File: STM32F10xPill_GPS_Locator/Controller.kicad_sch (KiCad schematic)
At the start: 38 parts, among them J2 Conn_01x03, J3 Conn_01x05, SW1 SW_Push, SW3 Button A, SW4 Button B, U1 STM32F100C4T6, Y1 16MHz, Y2 32.768kHz

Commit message: Updated net names, submit schematic for feedback
After feedback is incorporated, PCB layout is ready to begin
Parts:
- C1, C10, C2, C24, C25, C3, C4, C5, C6, C7, C8, C9: footprint (none) -> Capacitor_SMD:C_0402_1005Metric
- C11: footprint (none) -> Capacitor_SMD:C_0603_1608Metric
- D1: footprint (none) -> LED_SMD:LED_0603_1608Metric
- R1, R15, R17, R2, R3, R4, R5: footprint (none) -> Resistor_SMD:R_0402_1005Metric_Pad0.72x0.64mm_HandSolder
- TP1, TP2, TP3, TP4, TP5: footprint (none) -> TestPoint:TestPoint_Pad_D1.5mm
- TP17: value GPS_1PPS -> SCK; footprint (none) -> TestPoint:TestPoint_Pad_D1.5mm
- TP18: value GPS_1PPS -> SDA; footprint (none) -> TestPoint:TestPoint_Pad_D1.5mm
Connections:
- net BUTTON_B: now reaches C24.2, R17.1, SW4.2, U1.28 (PB15)
- net BUTTON_A: now reaches C25.2, R15.1, SW3.2, U1.27 (PB14)
- no-connect marks 0 -> 16
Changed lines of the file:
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@@
 		(color 0 0 0 0)
 	)
+	(no_connect
+		(at 195.58 207.01)
+	)
+	(no_connect
+		(at 231.14 109.22)
+	)
+	(no_connect
+		(at 231.14 127)
+	)
+	(no_connect
+		(at 231.14 116.84)
+	)
+	(no_connect
+		(at 231.14 106.68)
+	)
+	(no_connect
+		(at 231.14 111.76)
+	)
+	(no_connect
+		(at 231.14 124.46)
+	)
+	(no_connect
+		(at 195.58 194.31)
+	)
+	(no_connect
+		(at 195.58 189.23)
+	)
+	(no_connect
+		(at 231.14 99.06)
+	)
+	(no_connect
+		(at 231.14 104.14)
+	)
+	(no_connect
+		(at 231.14 121.92)
+	)
+	(no_connect
+		(at 231.14 114.3)
+	)
+	(no_connect
+		(at 231.14 129.54)
+	)
+	(no_connect
+		(at 231.14 101.6)
+	)
+	(no_connect
+		(at 231.14 119.38)
+	)
 	(wire
 		(pts
@@
 		)
 	)
+	(label "SDA"
+		(at 160.02 212.09 0)
+		(effects
+			(font
+				(size 1.27 1.27)
+			)
+			(justify left bottom)
+		)
+	)
 	(label "SWDIO"
 		(at 238.76 132.08 0)
@@
 		)
 	)
+	(label "BUTTON_A"
+		(at 165.1 233.68 0)
+		(effects
+			(font
+				(size 1.27 1.27)
+			)
+			(justify left bottom)
+		)
+	)
 	(label "OSCOUT"
 		(at 138.43 140.97 0)
@@
 		)
 	)
+	(label "BUTTON_B"
+		(at 165.1 245.11 0)
+		(effects
+			(font
+				(size 1.27 1.27)
+			)
+			(justify left bottom)
+		)
+	)
 	(label "MCU_BOOT0"
 		(at 184.15 107.95 0)
@@
 		)
 	)
+	(label "SCK"
+		(at 160.02 209.55 0)
+		(effects
+			(font
+				(size 1.27 1.27)
+			)
+			(justify left bottom)
+		)
+	)
 	(global_label "SDA"
 		(shape bidirectional)
@@
 			)
 		)
-		(property "Footprint" ""
+		(property "Footprint" "Capacitor_SMD:C_0402_1005Metric"
 			(at 260.6548 76.2 0)
 			(effects
@@
 			)
 		)
-		(property "Footprint" ""
+		(property "Footprint" "Resistor_SMD:R_0402_1005Metric_Pad0.72x0.64mm_HandSolder"
 			(at 146.304 228.346 90)
 			(effects
@@
 			)
 		)
-		(property "Footprint" ""
+		(property "Footprint" "Resistor_SMD:R_0402_1005Metric_Pad0.72x0.64mm_HandSolder"
 			(at 180.594 106.934 90)
 			(effects
@@
 			)
 		)
-		(property "Footprint" ""
+		(property "Footprint" "Capacitor_SMD:C_0603_1608Metric"
 			(at 197.1548 73.66 0)
 			(effects
@@
 			)
 		)
-		(property "Footprint" ""
+		(property "Footprint" "Capacitor_SMD:C_0402_1005Metric"
 			(at 147.0152 248.92 0)
 			(effects
@@
 			)
 		)
-		(property "Footprint" ""
+		(property "Footprint" "Capacitor_SMD:C_0402_1005Metric"
 			(at 119.38 117.1448 0)
 			(effects
@@
 			)
 		)
-		(property "Footprint" ""
+		(property "Footprint" "Capacitor_SMD:C_0402_1005Metric"
 			(at 249.2248 76.2 0)
 			(effects
@@
 			)
 		)
-		(property "Footprint" ""
+		(property "Footprint" "TestPoint:TestPoint_Pad_D1.5mm"
 			(at 172.72 139.7 0)
 			(effects
@@
 			)
 		)
-		(property "Footprint" ""
+		(property "Footprint" "Capacitor_SMD:C_0402_1005Metric"
 			(at 372.4148 67.31 0)
 			(effects
@@
 			)
 		)
-		(property "Value" "GPS_1PPS"
+		(property "Value" "SCK"
 			(at 130.81 204.978 90)
 			(effects
@@
 			)
 		)
-		(property "Footprint" ""
+		(property "Footprint" "TestPoint:TestPoint_Pad_D1.5mm"
 			(at 133.35 208.28 0)
 			(effects
@@
 			)
 		)
-		(property "Footprint" ""
+		(property "Footprint" "Capacitor_SMD:C_0402_1005Metric"
 			(at 119.38 157.7848 0)
 			(effects
@@
 			)
 		)
-		(property "Footprint" ""
+		(property "Footprint" "Capacitor_SMD:C_0402_1005Metric"
 			(at 119.38 140.0048 0)
 			(effects
@@
 			)
 		)
-		(property "Footprint" ""
+		(property "Footprint" "TestPoint:TestPoint_Pad_D1.5mm"
 			(at 143.51 57.15 0)
 			(effects
@@
 			)
 		)
-		(property "Footprint" ""
+		(property "Footprint" "Resistor_SMD:R_0402_1005Metric_Pad0.72x0.64mm_HandSolder"
 			(at 114.554 202.946 90)
 			(effects
@@
 			)
 		)
-		(property "Footprint" ""
+		(property "Footprint" "Capacitor_SMD:C_0402_1005Metric"
 			(at 119.38 173.0248 0)
 			(effects
@@
 			)
 		)
-		(property "Footprint" ""
+		(property "Footprint" "TestPoint:TestPoint_Pad_D1.5mm"
 			(at 172.72 172.72 0)
 			(effects
@@
 			)
 		)
-		(property "Footprint" ""
+		(property "Footprint" "Resistor_SMD:R_0402_1005Metric_Pad0.72x0.64mm_HandSolder"
 			(at 156.464 139.954 90)
 			(effects
@@
 			)
 		)
-		(property "Footprint" ""
+		(property "Footprint" "Resistor_SMD:R_0402_1005Metric_Pad0.72x0.64mm_HandSolder"
 			(at 253.746 173.736 90)
 			(effects
@@
 			)
 		)
-		(property "Footprint" ""
+		(property "Footprint" "Resistor_SMD:R_0402_1005Metric_Pad0.72x0.64mm_HandSolder"
 			(at 156.464 228.346 90)
 			(effects
@@
 			)
 		)
-		(property "Footprint" ""
+		(property "Footprint" "Capacitor_SMD:C_0402_1005Metric"
 			(at 127 67.0052 0)
 			(effects
@@
 			)
 		)
-		(property "Footprint" ""
+		(property "Footprint" "Capacitor_SMD:C_0402_1005Metric"
 			(at 226.3648 76.2 0)
 			(effects
@@
 			)
 		)
-		(property "Footprint" ""
+		(property "Footprint" "LED_SMD:LED_0603_1608Metric"
 			(at 283.21 172.72 0)
 			(effects
@@
 			)
 		)
-		(property "Footprint" ""
+		(property "Footprint" "Resistor_SMD:R_0402_1005Metric_Pad0.72x0.64mm_HandSolder"
 			(at 106.934 202.946 90)
 			(effects
@@
 			)
 		)
-		(property "Footprint" ""
+		(property "Footprint" "Capacitor_SMD:C_0402_1005Metric"
 			(at 237.7948 76.2 0)
 			(effects
@@
 			)
 		)
-		(property "Footprint" ""
+		(property "Footprint" "TestPoint:TestPoint_Pad_D1.5mm"
 			(at 172.72 116.84 0)
 			(effects
@@
 			)
 		)
-		(property "Footprint" ""
+		(property "Footprint" "Capacitor_SMD:C_0402_1005Metric"
 			(at 159.7152 248.92 0)
 			(effects
@@
 			)
 		)
-		(property "Footprint" ""
+		(property "Footprint" "TestPoint:TestPoint_Pad_D1.5mm"
 			(at 172.72 157.48 0)
 			(effects
@@
 			)
 		)
-		(property "Value" "GPS_1PPS"
+		(property "Value" "SDA"
 			(at 137.16 204.978 90)
 			(effects
@@
 			)
 		)
-		(property "Footprint" ""
+		(property "Footprint" "TestPoint:TestPoint_Pad_D1.5mm"
 			(at 139.7 208.28 0)
 			(effects

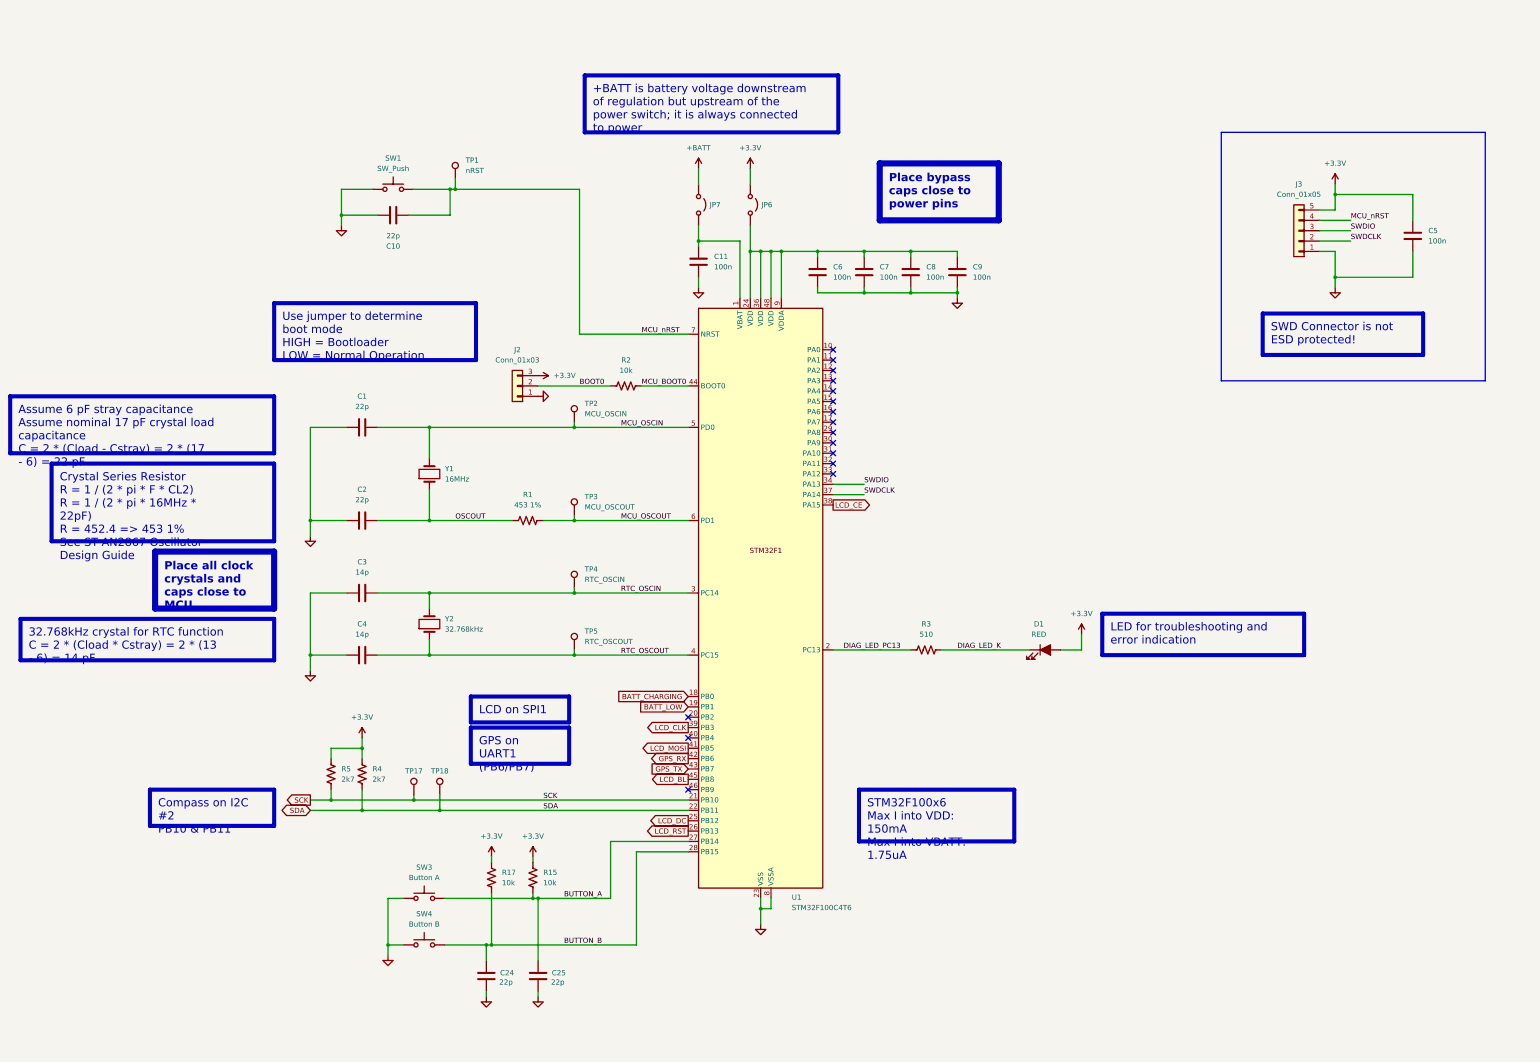
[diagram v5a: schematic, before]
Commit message: Add all footprints and symbols, retouch schametic
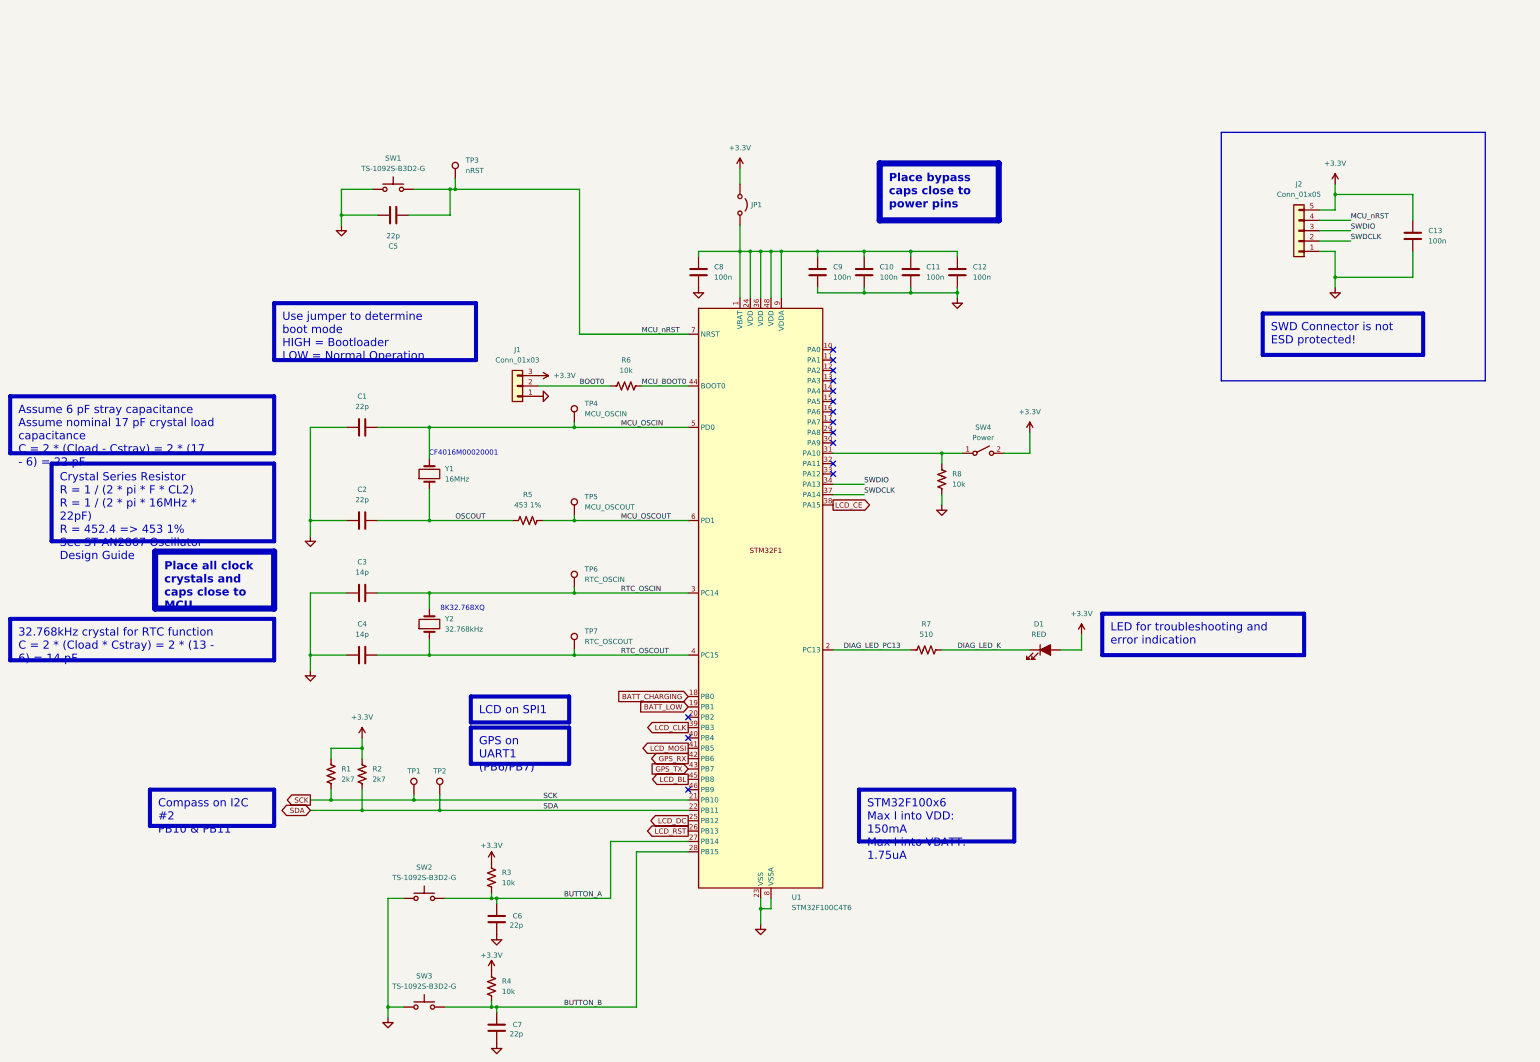
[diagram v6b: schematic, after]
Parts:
- removed JP7: Jumper_2_Open, symbol Jumper:Jumper_2_Open
- removed SW4: Button B, symbol Switch:SW_Push
- added R8: 10k, Resistor_SMD:R_0402_1005Metric_Pad0.72x0.64mm_HandSolder, symbol Device:R_US
- added SW2: TS-1092S-B3D2-G, Button_Switch_SMD:SW_Tactile_SPST_NO_Straight_CK_PTS636Sx25SMTRLFS, symbol Switch:SW_Push
- added SW4: Power, Connector_JST:JST_XH_B2B-XH-A_1x02_P2.50mm_Vertical, symbol Switch:SW_SPST
- J1: renamed from J2; footprint (none) -> Connector_PinHeader_2.54mm:PinHeader_1x03_P2.54mm_Vertical
- J2: renamed from J3; footprint (none) -> Connector_PinHeader_2.54mm:PinHeader_1x05_P2.54mm_Vertical
- JP1: renamed from JP6; footprint (none) -> Jumper:SolderJumper-2_P1.3mm_Open_Pad1.0x1.5mm
- SW1: value SW_Push -> TS-1092S-B3D2-G; footprint (none) -> Button_Switch_SMD:SW_Tactile_SPST_NO_Straight_CK_PTS636Sx25SMTRLFS; LCSC Part (none) -> C520860
- SW3: value Button A -> TS-1092S-B3D2-G; footprint (none) -> Button_Switch_SMD:SW_Tactile_SPST_NO_Straight_CK_PTS636Sx25SMTRLFS; LCSC Part (none) -> C520860
- Y1: footprint (none) -> Crystal:Crystal_SMD_3225-4Pin_3.2x2.5mm; LCSC Part (none) -> C7464895
- Y2: footprint (none) -> Crystal:Crystal_SMD_HC49-SD; LCSC Part (none) -> C19723458
- renumbered C7 to C10, C8 to C11, C9 to C12, C5 to C13, C10 to C5, C25 to C6, C24 to C7, C11 to C8, C6 to C9, R5 to R1, R4 to R2, R15 to R3, R17 to R4, R1 to R5, R2 to R6, R3 to R7, TP17 to TP1, TP18 to TP2, TP1 to TP3, TP2 to TP4, TP3 to TP5, TP4 to TP6, TP5 to TP7
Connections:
- net +3.3V: now also SW4.2 (B)
- net BUTTON_A: now also SW2.2; no longer SW3.2
- net BUTTON_B: now also SW3.2
- net GND: now also R8.1, SW2.1
- net MCU_OSCIN: now also Y1.3; no longer Y1.2
- net at C10.2, C11.2, C12.2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: now also C8.2, U1.1 (VBAT)
- net at U1.31 (PA10): now also R8.2, SW4.1 (A)
- no-connect marks 16 -> 15
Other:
- note added: "8K32.768XQ"
- note added: "CF4016M00020001"
- moved on the sheet: C6, C7, C8, JP1, R3, R4

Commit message: Begin PCB layout
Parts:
- removed SW1: TS-1092S-B3D2-G, Button_Switch_SMD:SW_Tactile_SPST_NO_Straight_CK_PTS636Sx25SMTRLFS, symbol Switch:SW_Push
- removed TP4: MCU_OSCIN, TestPoint:TestPoint_Pad_D1.5mm, symbol Connector:TestPoint
- removed TP5: MCU_OSCOUT, TestPoint:TestPoint_Pad_D1.5mm, symbol Connector:TestPoint
- removed TP6: RTC_OSCIN, TestPoint:TestPoint_Pad_D1.5mm, symbol Connector:TestPoint
- removed TP7: RTC_OSCOUT, TestPoint:TestPoint_Pad_D1.5mm, symbol Connector:TestPoint
- added C27: 22p, Capacitor_SMD:C_0402_1005Metric, symbol Device:C
- added R24: 10k, Resistor_SMD:R_0402_1005Metric_Pad0.72x0.64mm_HandSolder, symbol Device:R_US
- added SW5: TS-1092S-B3D2-G, Button_Switch_SMD:SW_Tactile_SPST_NO_Straight_CK_PTS636Sx25SMTRLFS, symbol Switch:SW_Push
- added SW6: PTS645VH58-2 LFS, Button_Switch_THT:SW_Tactile_SPST_Angled_PTS645Vx58-2LFS, symbol Switch:SW_Push
- J1: footprint Connector_PinHeader_2.54mm:PinHeader_1x03_P2.54mm_Vertical -> Connector_PinHeader_2.54mm:PinHeader_1x03_P2.54mm_Horizontal
- J2: footprint Connector_PinHeader_2.54mm:PinHeader_1x05_P2.54mm_Vertical -> Connector_PinHeader_2.54mm:PinHeader_1x05_P2.54mm_Horizontal
- SW4: footprint Connector_JST:JST_XH_B2B-XH-A_1x02_P2.50mm_Vertical -> Connector_JST:JST_PH_B2B-PH-K_1x02_P2.00mm_Vertical
- Y2: footprint Crystal:Crystal_SMD_HC49-SD -> Crystal:Crystal_SMD_3215-2Pin_3.2x1.5mm; LCSC Part C19723458 -> C5361379
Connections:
- net +3.3V: now also R24.2
- net BUTTON_B: now also U1.31 (PA10), C27.2, R24.1, SW5.2; no longer C7.2, R4.1, SW3.2, U1.28 (PB15)
- net GND: now also C27.1, SW5.1, SW6.1
- net MCU_nRST: now also SW6.2
- net MCU_VDD: now reaches C10.2, C11.2, C12.2, C8.2, C9.2, JP1.2 (B), U1.1 (VBAT), U1.24 (VDD), U1.36 (VDD), U1.48 (VDD), U1.9 (VDDA)
- net POWER_SWITCH: now reaches U1.10 (PA0)
- net POWER_SWITCH: now also R8.2, SW4.1 (A)
- new net BUTTON_C: C7.2, R4.1, SW3.2, U1.28 (PB15)
- no-connect marks 15 -> 14
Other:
- note added: "H31003271C2070CY"
- note removed: "8K32.768XQ"
- moved on the sheet: C13, J2, R8, SW4

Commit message: Initial placement completed
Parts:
- renumbered C27 to C13, C13 to C14, R24 to R9, SW6 to SW1
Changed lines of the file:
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@@
 		(dnp no)
 		(fields_autoplaced yes)
-		(property "Reference" "R24"
+		(property "Reference" "R9"
 			(at 274.32 118.11 0)
 			(effects
@@
 			(project "STM32F10xPill_GPS_Locator"
 				(path "/ea8b3ef8-8ecc-4b82-8187-a133f9b3c76f/dfffea79-d379-47b9-be13-2a2070f80d43"
-					(reference "R24")
+					(reference "R9")
 					(unit 1)
 				)
@@
 		(on_board yes)
 		(dnp no)
-		(property "Reference" "#PWR017"
+		(property "Reference" "#PWR019"
 			(at 279.4 100.33 0)
 			(effects
@@
 			(project "STM32F10xPill_GPS_Locator"
 				(path "/ea8b3ef8-8ecc-4b82-8187-a133f9b3c76f/dfffea79-d379-47b9-be13-2a2070f80d43"
-					(reference "#PWR017")
+					(reference "#PWR019")
 					(unit 1)
 				)
@@
 		(on_board yes)
 		(dnp no)
-		(property "Reference" "C27"
+		(property "Reference" "C13"
 			(at 270.51 128.778 0)
 			(effects
@@
 			(project "STM32F10xPill_GPS_Locator"
 				(path "/ea8b3ef8-8ecc-4b82-8187-a133f9b3c76f/dfffea79-d379-47b9-be13-2a2070f80d43"
-					(reference "C27")
+					(reference "C13")
 					(unit 1)
 				)
@@
 		(dnp no)
 		(fields_autoplaced yes)
-		(property "Reference" "#PWR058"
+		(property "Reference" "#PWR021"
 			(at 302.26 133.35 0)
 			(effects
@@
 			(project "STM32F10xPill_GPS_Locator"
 				(path "/ea8b3ef8-8ecc-4b82-8187-a133f9b3c76f/dfffea79-d379-47b9-be13-2a2070f80d43"
-					(reference "#PWR058")
+					(reference "#PWR021")
 					(unit 1)
 				)
@@
 		(dnp no)
 		(fields_autoplaced yes)
-		(property "Reference" "C13"
+		(property "Reference" "C14"
 			(at 388.62 39.37 0)
 			(effects
@@
 			(project "STM32F10xPill_GPS_Locator"
 				(path "/ea8b3ef8-8ecc-4b82-8187-a133f9b3c76f/dfffea79-d379-47b9-be13-2a2070f80d43"
-					(reference "C13")
+					(reference "C14")
 					(unit 1)
 				)
@@
 		(dnp no)
 		(fields_autoplaced yes)
-		(property "Reference" "#PWR018"
+		(property "Reference" "#PWR020"
 			(at 292.1 172.72 0)
 			(effects
@@
 			(project "STM32F10xPill_GPS_Locator"
 				(path "/ea8b3ef8-8ecc-4b82-8187-a133f9b3c76f/dfffea79-d379-47b9-be13-2a2070f80d43"
-					(reference "#PWR018")
+					(reference "#PWR020")
 					(unit 1)
 				)
@@
 		(on_board yes)
 		(dnp no)
-		(property "Reference" "#PWR059"
+		(property "Reference" "#PWR018"
 			(at 276.86 119.38 0)
 			(effects
@@
 			(project "STM32F10xPill_GPS_Locator"
 				(path "/ea8b3ef8-8ecc-4b82-8187-a133f9b3c76f/dfffea79-d379-47b9-be13-2a2070f80d43"
-					(reference "#PWR059")
+					(reference "#PWR018")
 					(unit 1)
 				)
@@
 		(dnp no)
 		(fields_autoplaced yes)
-		(property "Reference" "#PWR020"
+		(property "Reference" "#PWR023"
 			(at 365.76 59.69 0)
 			(effects
@@
 			(project "STM32F10xPill_GPS_Locator"
 				(path "/ea8b3ef8-8ecc-4b82-8187-a133f9b3c76f/dfffea79-d379-47b9-be13-2a2070f80d43"
-					(reference "#PWR020")
+					(reference "#PWR023")
 					(unit 1)
 				)
@@
 		(dnp no)
 		(fields_autoplaced yes)
-		(property "Reference" "#PWR060"
+		(property "Reference" "#PWR017"
 			(at 275.59 139.7 0)
 			(effects
@@
 			(project "STM32F10xPill_GPS_Locator"
 				(path "/ea8b3ef8-8ecc-4b82-8187-a133f9b3c76f/dfffea79-d379-47b9-be13-2a2070f80d43"
-					(reference "#PWR060")
+					(reference "#PWR017")
 					(unit 1)
 				)
@@
 		(dnp no)
 		(fields_autoplaced yes)
-		(property "Reference" "#PWR019"
+		(property "Reference" "#PWR022"
 			(at 365.76 31.75 0)
 			(effects
@@
 			(project ""
 				(path "/ea8b3ef8-8ecc-4b82-8187-a133f9b3c76f/dfffea79-d379-47b9-be13-2a2070f80d43"
-					(reference "#PWR019")
+					(reference "#PWR022")
 					(unit 1)
 				)
@@
 		(dnp no)
 		(fields_autoplaced yes)
-		(property "Reference" "SW6"
+		(property "Reference" "SW1"
 			(at 123.19 52.07 0)
 			(effects
@@
 			(project "STM32F10xPill_GPS_Locator"
 				(path "/ea8b3ef8-8ecc-4b82-8187-a133f9b3c76f/dfffea79-d379-47b9-be13-2a2070f80d43"
-					(reference "SW6")
+					(reference "SW1")
 					(unit 1)
 				)
